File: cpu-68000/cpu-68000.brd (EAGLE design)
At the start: 149.9 x 99.7 mm, 69 parts, among them IC201 AS6C4008, IC202 AS6C4008, IC203 39SF040, IC204 39SF040, IC301 XR68C681, IC302 DS1244Y, IC303 MAX232, IC401 GAL22V10, IC402 GAL22V10, IC403 LM3724, IC404 74HC175D, J201 POWER_JACK, Q301 3.6864 MHz

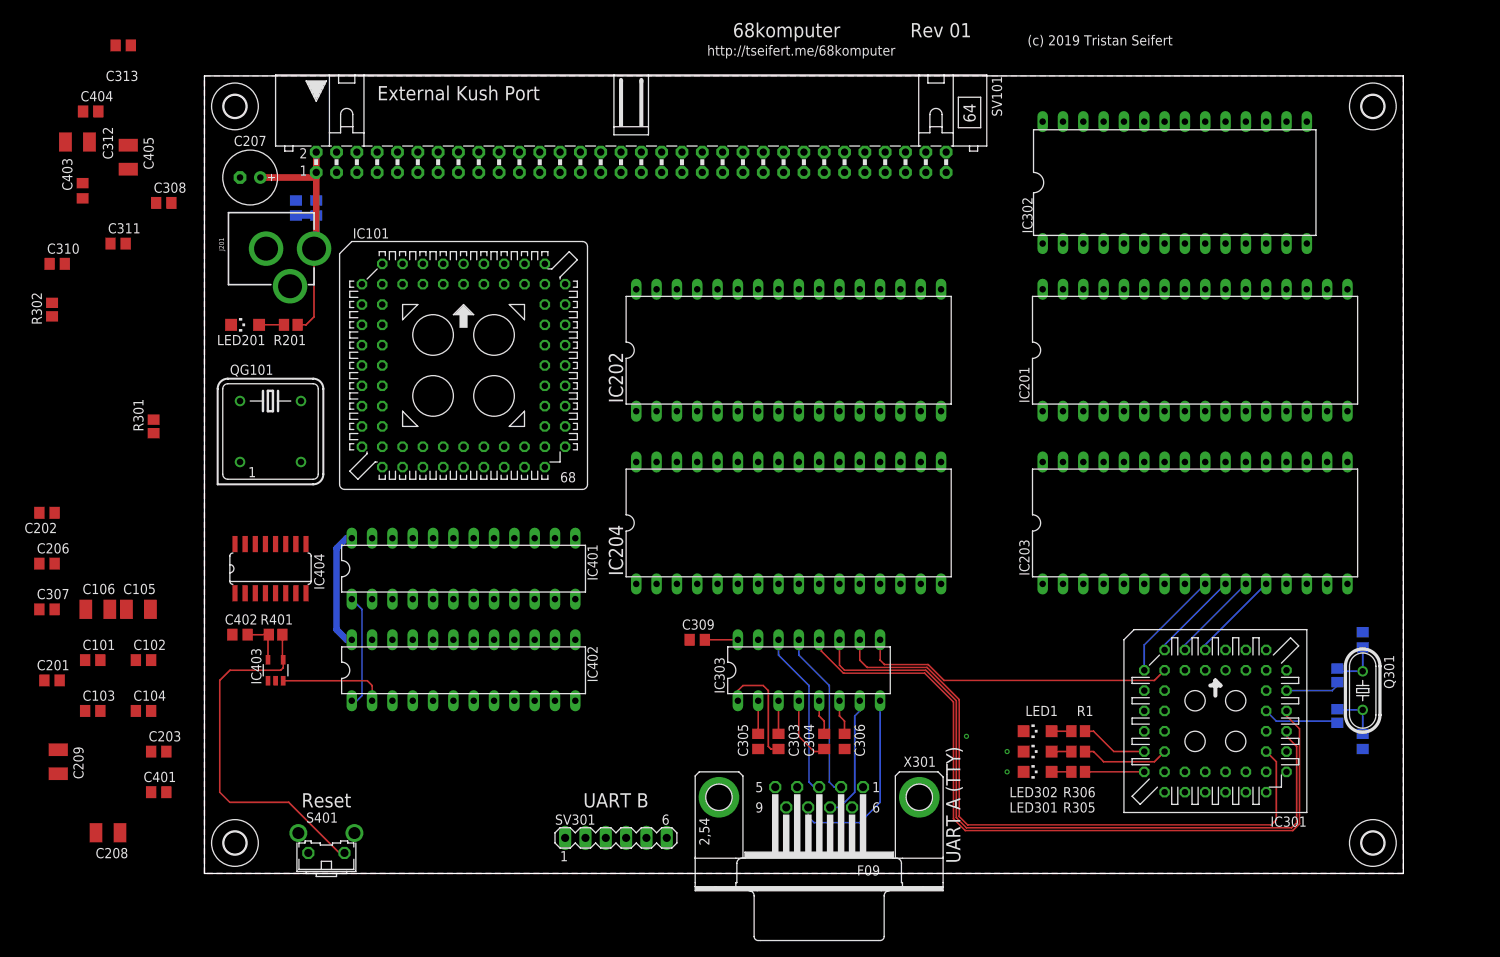
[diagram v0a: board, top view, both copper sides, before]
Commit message: finished routing basic busses and some control signals
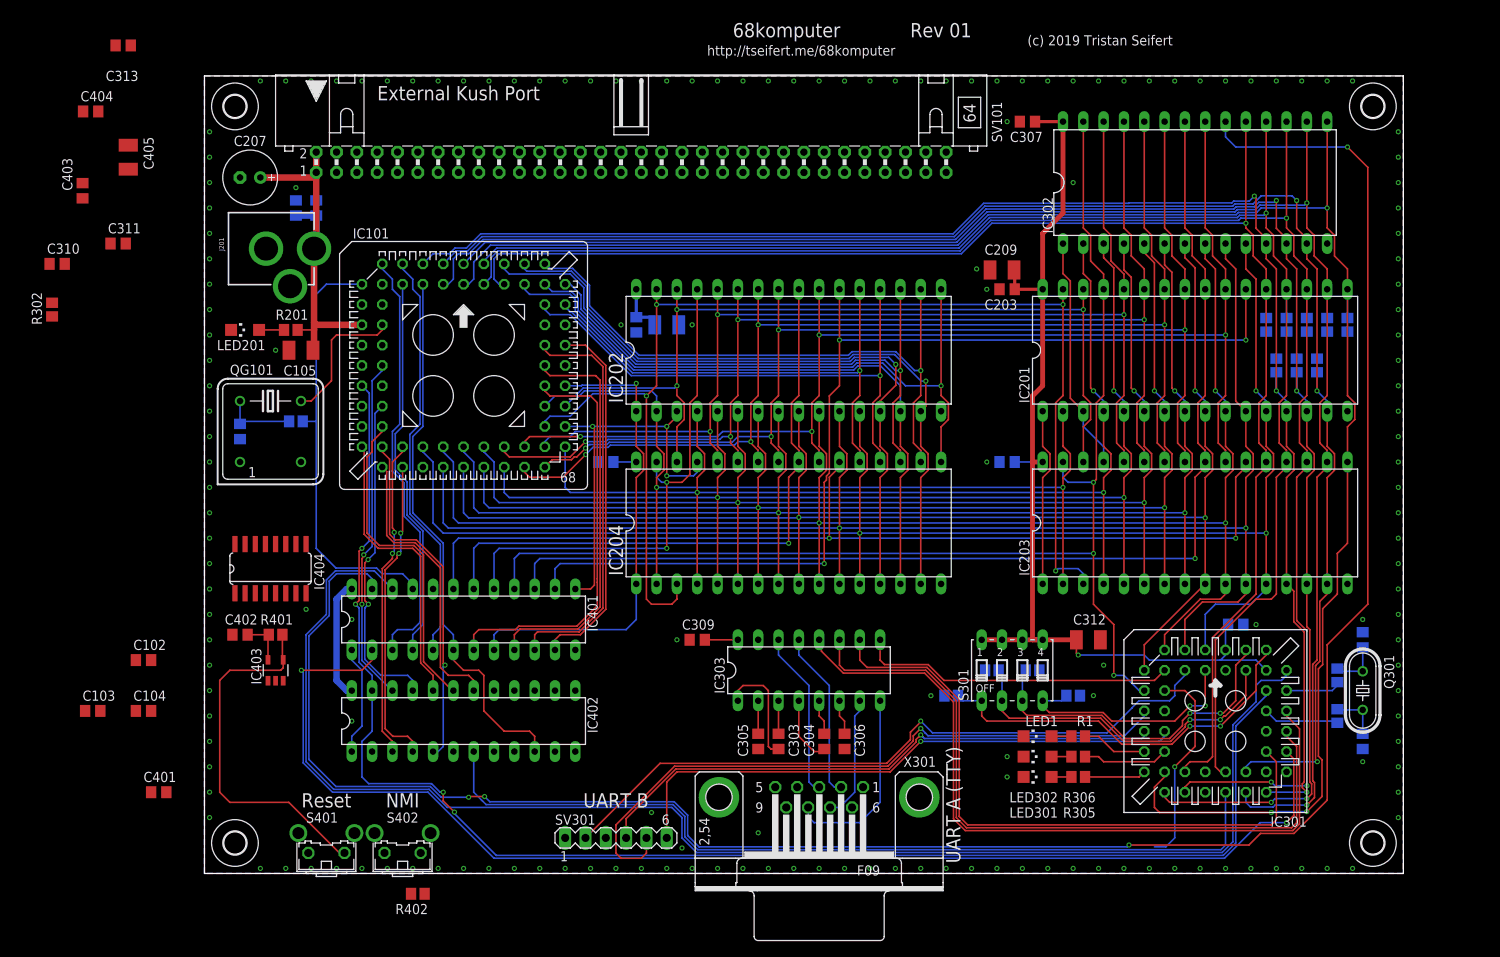
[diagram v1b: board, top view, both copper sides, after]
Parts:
- removed C106: 10µF, rcl:SMC_B
- removed R301: 10k, rcl:R2012
- added R10, R11, R12, R13, R14, R2, R3, R4, R402, R5, R6, R7, R8, R9: 10k, rcl:R2012
- added S301: (no value), switch-dil:DIP04S
- added S402: (no value), switch-omron:B3F-31XX
- moved C308 144.0 mm to (128.9, 31.1), flipped to the bottom, turned to 180 degrees
- moved C312 140.9 mm to (110.5, 29.2), turned to 0 degrees
- moved C307 136.9 mm to (102.9, 94.0), turned to 180 degrees
- moved C209 133.0 mm to (99.7, 75.4), turned to 180 degrees
- moved C203 120.8 mm to (100.3, 73.0), turned to 180 degrees
- moved C206 120.7 mm to (100.3, 51.4), flipped to the bottom
- moved C208 94.4 mm to (57.8, 68.6), flipped to the bottom, turned to 180 degrees
- moved C201 85.5 mm to (54.0, 68.6), flipped to the bottom, turned to 270 degrees
- moved C202 70.1 mm to (50.2, 51.4), flipped to the bottom, turned to 0 degrees
- moved C105 38.2 mm to (12.1, 65.4), turned to 180 degrees
- moved C101 34.0 mm to (4.45, 55.2), flipped to the bottom, turned to 270 degrees
- moved IC401 6.35 mm to (32.4, 31.8)
- moved IC402 6.35 mm to (32.4, 19.1)
- moved IC302 2.54 mm to (123.8, 86.4)
- moved LED201 0.64 mm to (5.08, 67.9)
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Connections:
- net !EXTIRQ renamed !EXTI_A
- removed net !68681_DTACK: R301.1
- removed net !IACK: IC402.16, IC402.9
- removed net N$14: IC402.21
- removed net N$15: IC402.22
- removed net N$16: IC402.23
- new net !EXTI_B: IC402.9
- new net CONF0: IC301.40, R11.2, S301.1
- new net CONF1: IC301.43, R12.2, S301.2
- new net CONF2: IC301.42, R13.2, S301.3
- new net CONF3: IC301.3, R14.2, S301.4
- net !AS: now also IC401.6; no longer IC401.13
- net !BERR_TIMER_CLR: now also IC402.14; no longer IC401.15
- net !DTACK: now also IC401.21, R2.1; no longer IC401.14
- net !HALT: now also IC402.22; no longer IC402.15
- net !IPL0: now also IC402.18; no longer IC402.17
- net !IPL1: now also IC402.20; no longer IC402.18
- net !LDS: now also IC401.4; no longer IC401.11
- net !LOE: now also IC401.15; no longer IC401.18
- net !LWE: now also IC301.9, IC401.16; no longer IC401.17
- net !NMI: now also R402.2, S402.2
- net !RAM_CS: now also IC401.14; no longer IC401.21
- net !RESET: now also IC402.23; no longer IC402.14
- net !ROM_CS: now also IC401.19; no longer IC401.20
- net !UDS: now also IC401.5; no longer IC401.10
- net !UOE: now also IC401.18; no longer IC401.19
- net !UWE: now also IC401.17; no longer IC401.16
- net !VPA: now also IC402.21; no longer IC402.20
- net +5V: now also R2.2, R402.1, S301.5, S301.6, S301.7, S301.8; no longer C106.+, R301.2
- net A15: now also IC401.13
- net A18: no longer IC401.8
- net A19: now also IC401.8; no longer IC401.7
- net A20: now also IC401.7; no longer IC401.6
- net A21: now also IC401.9; no longer IC401.5
- net A22: now also IC401.11; no longer IC401.4
- net A23: now also IC401.10; no longer IC401.3
- net D0: now also R3.2
- net D1: now also R4.2
- net D2: now also R5.2
- net D3: now also R6.2
- net D4: now also R7.2
- net D5: now also R8.2
- net D6: now also R9.2
- net D7: now also R10.2
- net GND: now also R10.1, R11.1, R12.1, R13.1, R14.1, R3.1, R4.1, R5.1, R6.1, R7.1, R8.1, R9.1, S402.1; no longer C106.-
- net R/!W!: now also IC401.3; no longer IC301.9, IC401.9
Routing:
- net !RTC_CS: track 0.00 -> 268.9 mm, vias 0 -> 4
- net D3: track 0.00 -> 231.6 mm, vias 0 -> 3
- net D5: track 0.00 -> 211.0 mm, vias 0 -> 3
- net D4: track 0.00 -> 209.9 mm, vias 0 -> 2
- net D1: track 0.00 -> 208.8 mm, vias 0 -> 4
- net D2: track 0.00 -> 195.8 mm, vias 0 -> 3
- net D6: track 0.00 -> 193.0 mm, vias 0 -> 1
- net D0: track 0.00 -> 193.0 mm, vias 0 -> 3
- net D7: track 0.00 -> 192.1 mm, vias 0 -> 1
- net !RESET: track 0.00 -> 186.7 mm, vias 0 -> 4
- net A1: track 11.4 -> 195.4 mm, vias 0 -> 3
- net !68681_CS: track 0.00 -> 181.7 mm
- net A2: track 11.4 -> 188.3 mm, vias 0 -> 2
- net A3: track 11.4 -> 185.8 mm, vias 0 -> 3
- net A4: track 14.0 -> 179.4 mm, vias 0 -> 3
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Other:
- board text added: "NMI"

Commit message: completed routing of basic 68000 board; needs expansion bus connector routing
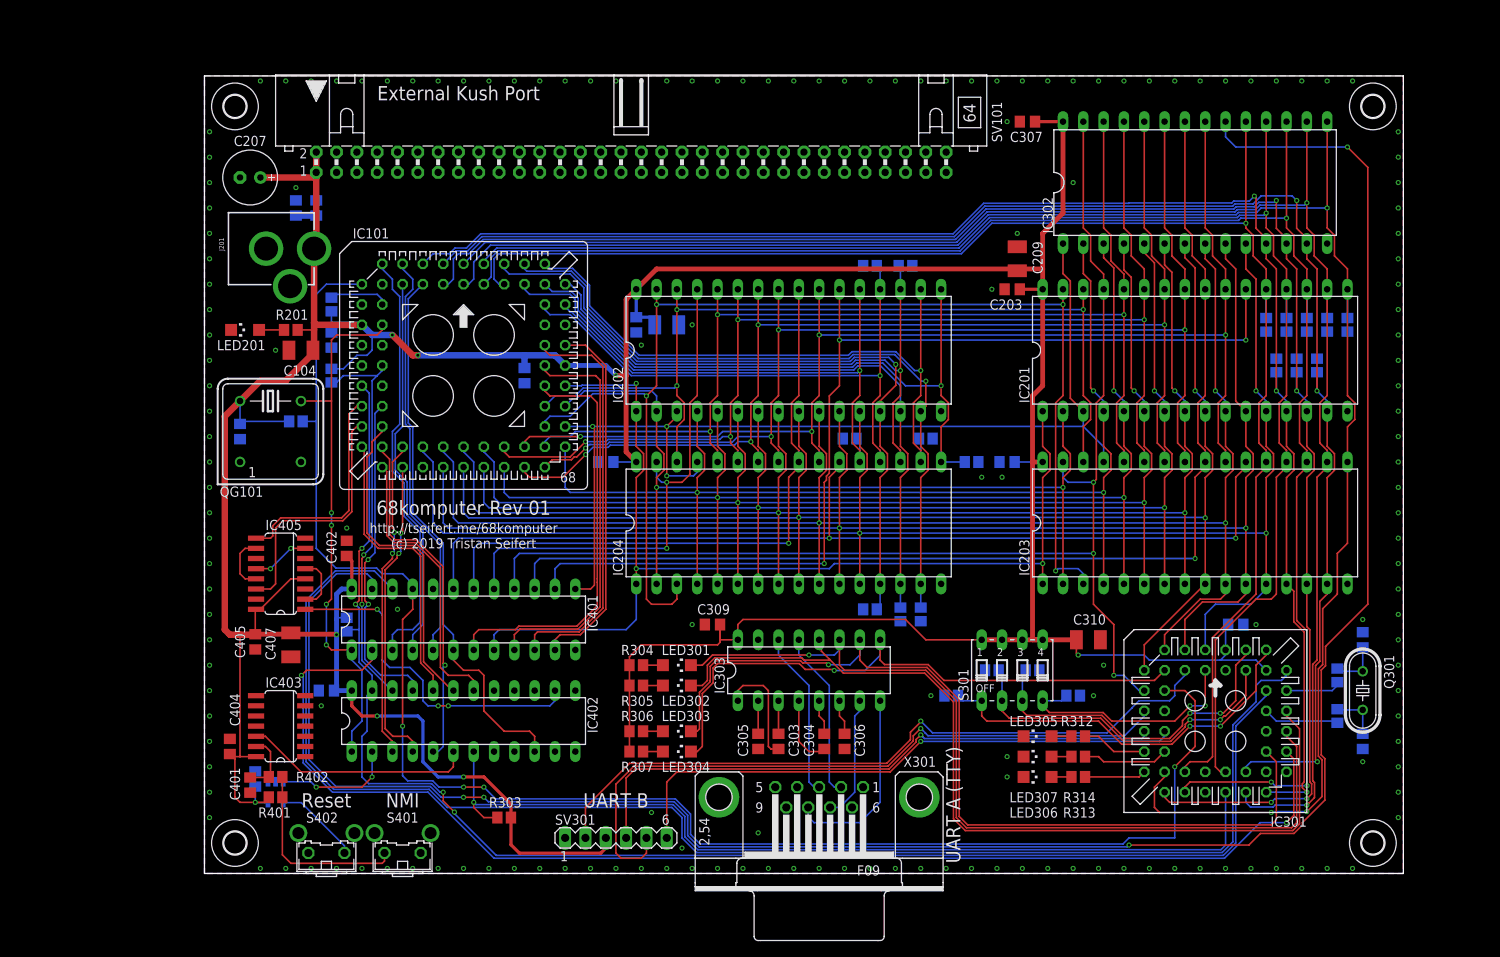
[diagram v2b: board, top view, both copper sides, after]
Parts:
- removed C105, C312: 10µF, rcl:SMC_B
- removed C311, C313: 100nF, rcl:C0805
- added C406: 100nF, rcl:C0805
- added C407: 10µF, rcl:SMC_B
- added IC405: 74HC175D, 74xx-eu:SO16
- added LED303, LED304, LED306, LED307: (no value), led:CHIPLED_1206
- added R101, R102, R103, R104, R105, R106, R107, R108, R109, R110: 10k, rcl:R2012
- added R301: 100R, rcl:R2012
- added R307, R312, R313, R314: 3k, rcl:R2012
- C104, C310: value 100nF -> 10µF; device rcl:C0805 -> rcl:SMC_B
- C401: value 100nF -> 10µF
- C405: value 10µF -> 100nF; device rcl:SMC_B -> rcl:C0805
- IC403: value LM3724 -> 74HC14D; device 68komputer:SOT23-5 -> 74xx-eu:SO14
- IC404: value 74HC175D -> LM3724; device 74xx-eu:SO16 -> 68komputer:SOT23-5
- R1: value 3k -> 10k
- R302, R402: value 10k -> 100R
- R303: value 100R -> 10k
- R304: value 100R -> 3k
- moved R302 167.0 mm to (141.6, 24.8), flipped to the bottom, turned to 270 degrees
- moved C310 137.2 mm to (110.5, 29.2)
- moved R303 105.6 mm to (37.5, 6.99), flipped to the top, turned to 0 degrees
- moved R304 87.9 mm to (54.0, 26.0), flipped to the top, turned to 180 degrees
- moved C404 81.3 mm to (3.17, 15.9), turned to 90 degrees
- moved R2 79.3 mm to (87.0, 32.4), turned to 90 degrees
- moved C403 69.5 mm to (15.2, 22.9), flipped to the bottom, turned to 0 degrees
- moved C103 68.3 mm to (40.0, 62.2), flipped to the bottom, turned to 270 degrees
- moved C405 62.6 mm to (6.35, 29.0), turned to 270 degrees
- moved R8 58.9 mm to (80.6, 54.4), turned to 180 degrees
- moved R7 57.6 mm to (83.2, 75.9), turned to 180 degrees
- moved R305 56.4 mm to (54.0, 23.5)
- moved R6 55.7 mm to (87.6, 75.9), turned to 0 degrees
- moved R306 55.3 mm to (54.0, 17.8)
- moved R3 54.3 mm to (89.5, 32.4), turned to 90 degrees
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- renumbered LED1 to LED305, R10 to R112, R11 to R308, R12 to R309, R13 to R310, R14 to R311, R9 to R111
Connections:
- new net N$11: R401.2, R402.1, S401.1
- new net N$12: LED301.A, R304.1
- new net N$13: C401.1, IC403.13, R402.2
- new net N$14: LED302.A, R305.1
- new net N$15: LED303.A, R306.1
- new net N$16: LED304.A, R307.1
- net !68681_IRQ: now also R303.1; no longer R302.1
- net !A_CTS: now also LED304.C
- net !A_RTS: now also LED303.C
- net !BERR: now also IC405.14; no longer IC404.14
- net !BERR_TIMER_CLR: now also IC405.1; no longer IC404.1
- net !BR: now also R104.1
- net !DTACK: now also R101.1; no longer R2.1
- net !HALT: now also R103.1
- net !MR: now also IC404.4, S402.2; no longer IC403.4, R401.2, S401.2
- net !NMI: now also IC403.12; no longer R402.2, S402.2
- net !RESET: now also R102.1
- net !RESET_IN: now also IC404.3; no longer IC403.3
- net +5V: now also C104.+, C310.+, C405.1, C406.1, C407.+, IC403.14, IC404.5, IC405.16, IC405.4, R101.2, R102.2, R103.2, R104.2, R303.2, R304.2, R305.2, R306.2, R307.2; no longer C104.1, C105.+, C310.1, C311.1, C312.+, C313.1, C401.1, C405.+, IC403.5, IC404.16, IC404.4, R2.2, R302.2, R402.1
- net 68681_X1: now also R301.2; no longer R304.2
- net 68681_X2: now also R302.2; no longer R303.2
- net A_RX: now also LED302.C
- net A_TX: now also LED301.C
- net D0: now also R105.2; no longer R3.2
- net D1: now also R106.2; no longer R4.2
- net D10: now also R3.2
- net D11: now also R4.2
- net D12: now also R5.2
- net D13: now also R6.2
- net D14: now also R7.2
- net D15: now also R8.2
- net D2: now also R107.2; no longer R5.2
- net D3: now also R108.2; no longer R6.2
- net D4: now also R109.2; no longer R7.2
- net D5: now also R110.2; no longer R8.2
- net D8: now also R1.2
- net D9: now also R2.2
- net E: now also IC405.9; no longer IC404.9
- net GND: now also C104.-, C310.-, C405.2, C406.2, C407.-, IC403.11, IC403.3, IC403.5, IC403.7, IC403.9, IC404.1, IC404.2, IC405.8, LED306.C, LED307.C, R1.1, R105.1, R106.1, R107.1, R108.1, R109.1, R110.1, R2.1, S401.2; no longer C104.2, C105.-, C310.2, C311.2, C312.-, C313.2, C405.-, IC403.2, IC404.8, LED301.C, LED302.C, S401.1
- net N$10: now also R312.2; no longer R1.2
- net N$2: now also C301.2, R301.1; no longer C302.2, R304.1
- net N$3: now also C302.2, R302.1; no longer C301.2, R303.1
- net N$5: now also IC405.2, IC405.5; no longer IC404.2, IC404.5
- net N$6: now also IC405.12, IC405.7; no longer IC404.12, IC404.7
- net N$7: now also LED306.A, R313.2; no longer LED301.A, R305.2
- net N$8: now also IC405.10, IC405.13; no longer IC404.10, IC404.13
- net N$9: now also LED307.A, R314.2; no longer LED302.A, R306.2
- net STATUS0: now also R314.1; no longer R306.1
- net STATUS1: now also R313.1; no longer R305.1
- net STATUS2: now also R312.1; no longer R1.1
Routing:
- net +5V: track 215.3 -> 549.1 mm, vias 1 -> 8
- net !DTACK: track 79.8 -> 202.5 mm, vias 1 -> 4
- net A15: track 78.5 -> 130.6 mm
- net A19: track 82.1 -> 133.2 mm, vias 1 -> 3
- net !BERR_TIMER_CLR: track 0.00 -> 42.6 mm, vias 0 -> 3
- net !A_CTS: track 39.7 -> 75.9 mm, vias 0 -> 1
- net CLK: track 31.2 -> 66.9 mm, vias 0 -> 4
- net !MR: track 45.5 -> 10.8 mm
- net !BERR: track 0.00 -> 31.6 mm
- net !A_RTS: track 81.0 -> 112.2 mm, vias 0 -> 1
- net !NMI: track 0.00 -> 28.7 mm
- net E: track 0.00 -> 27.9 mm
- net N$11: track 0.00 -> 24.1 mm
- net A_TX: track 89.5 -> 110.1 mm, vias 0 -> 1
- net A_RX: track 94.3 -> 114.3 mm
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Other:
- board text added: "68komputer Rev 01"
- board text removed: "68komputer"
- board text removed: "Rev 01"
